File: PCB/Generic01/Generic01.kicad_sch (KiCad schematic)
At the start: 3 parts, among them J1 Header, U1 ESP32-PICO-MINI-02

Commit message: Production files
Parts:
- J1: JLCPCB Position Offset (none) -> 3.81,-1.27; JLCPCB Rotation Offset (none) -> 90; LCSC Part # (none) -> v

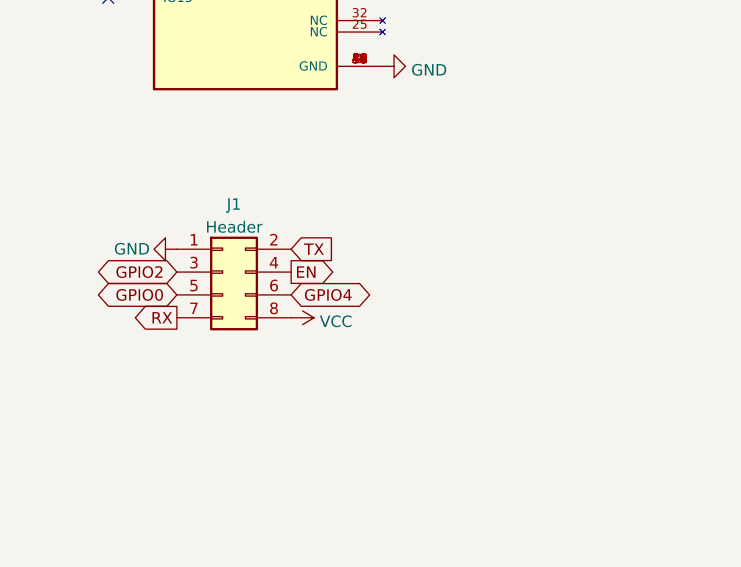
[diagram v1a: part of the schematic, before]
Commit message: Move RST
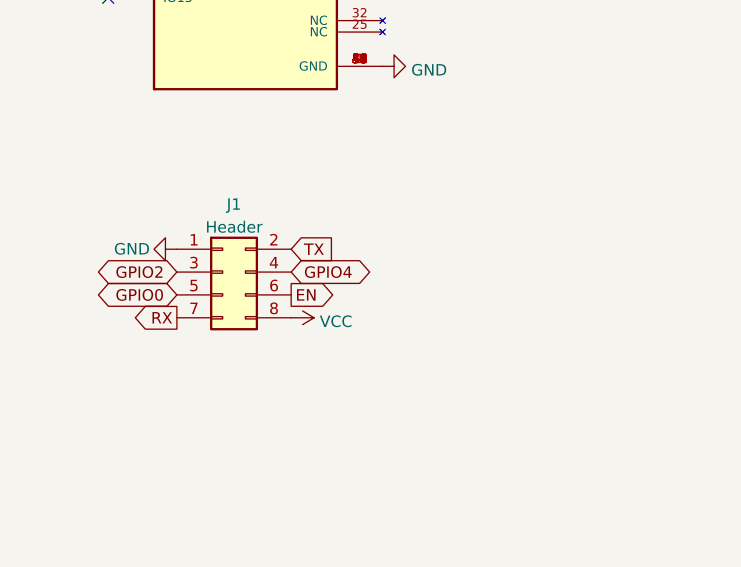
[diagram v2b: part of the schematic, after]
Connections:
- net EN: now also J1.6 (Pin_6); no longer J1.4 (Pin_4)
- net GPIO4: now also J1.4 (Pin_4); no longer J1.6 (Pin_6)
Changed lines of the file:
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@@
     )
   )
-  (global_label "EN" (shape output) (at 129.54 132.08 0) (fields_autoplaced)
+  (global_label "EN" (shape output) (at 129.54 134.62 0) (fields_autoplaced)
     (effects (font (size 1.27 1.27)) (justify left))
-    (property "Intersheetrefs" "${INTERSHEET_REFS}" (at 134.3437 132.0006 0)
+    (property "Intersheetrefs" "${INTERSHEET_REFS}" (at 134.3437 134.5406 0)
       (effects (font (size 1.27 1.27)) (justify left) hide)
     )
@@
     )
   )
-  (global_label "GPIO4" (shape bidirectional) (at 129.54 134.62 0) (fields_autoplaced)
+  (global_label "GPIO4" (shape bidirectional) (at 129.54 132.08 0) (fields_autoplaced)
     (effects (font (size 1.27 1.27)) (justify left))
-    (property "Intersheetrefs" "${INTERSHEET_REFS}" (at 137.549 134.6994 0)
+    (property "Intersheetrefs" "${INTERSHEET_REFS}" (at 137.549 132.1594 0)
       (effects (font (size 1.27 1.27)) (justify left) hide)
     )

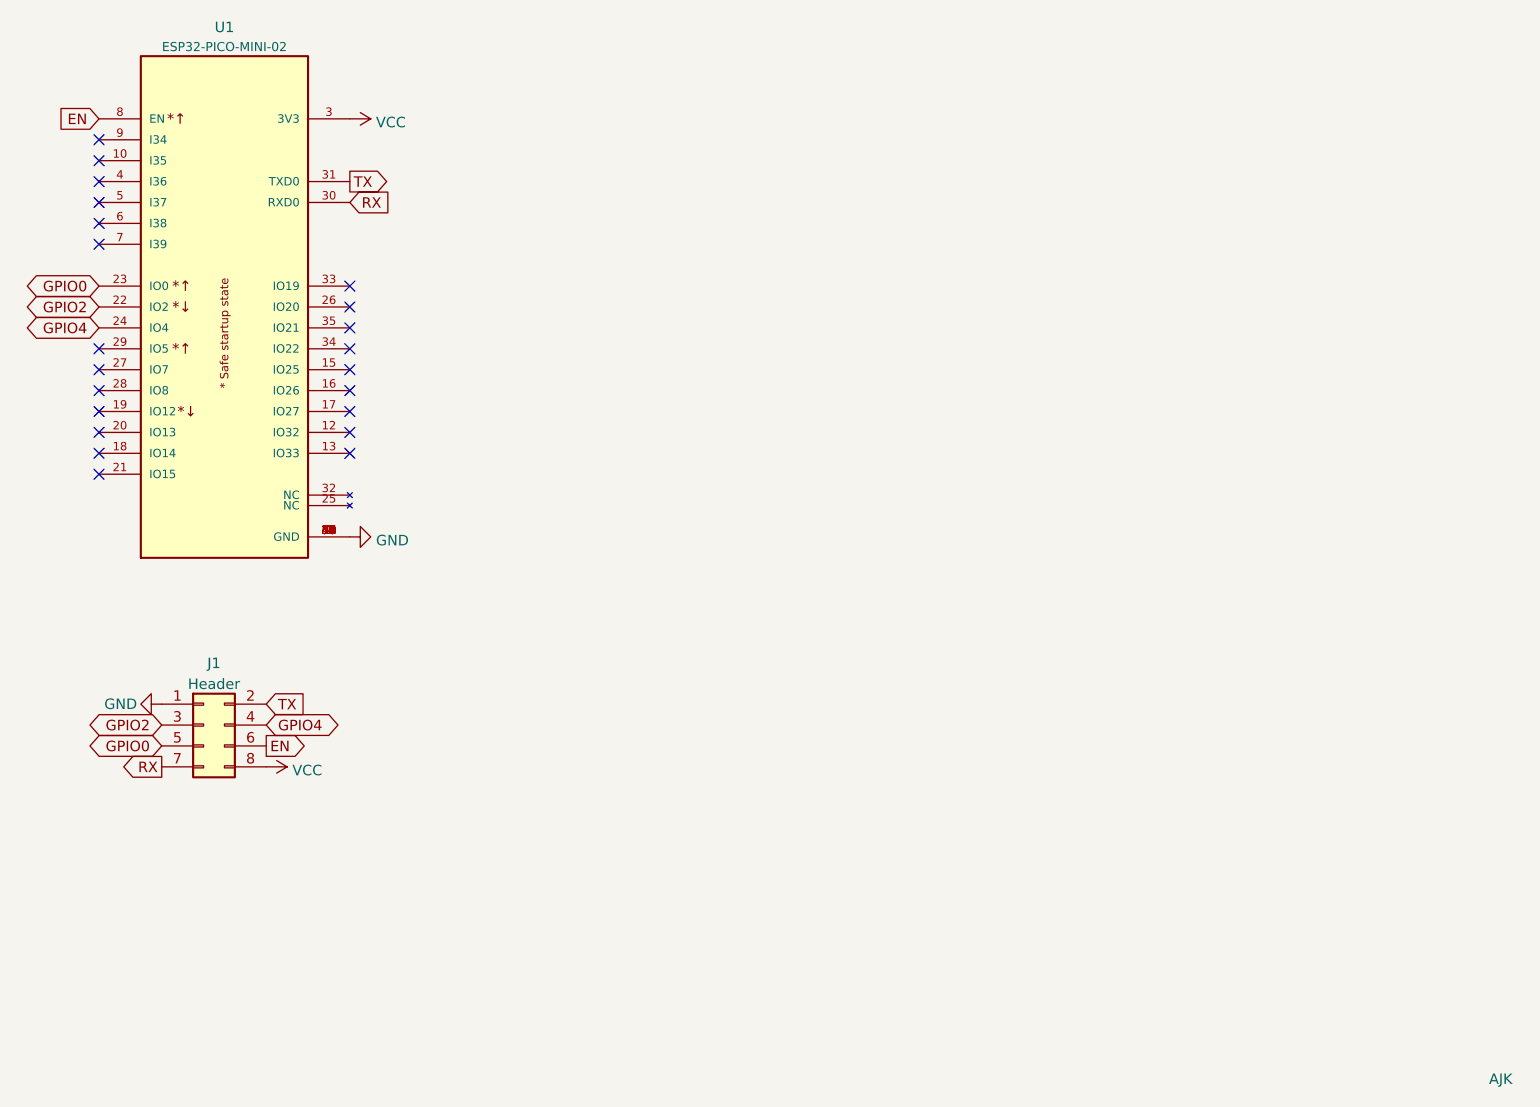
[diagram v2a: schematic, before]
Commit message: Tidy RST as EN
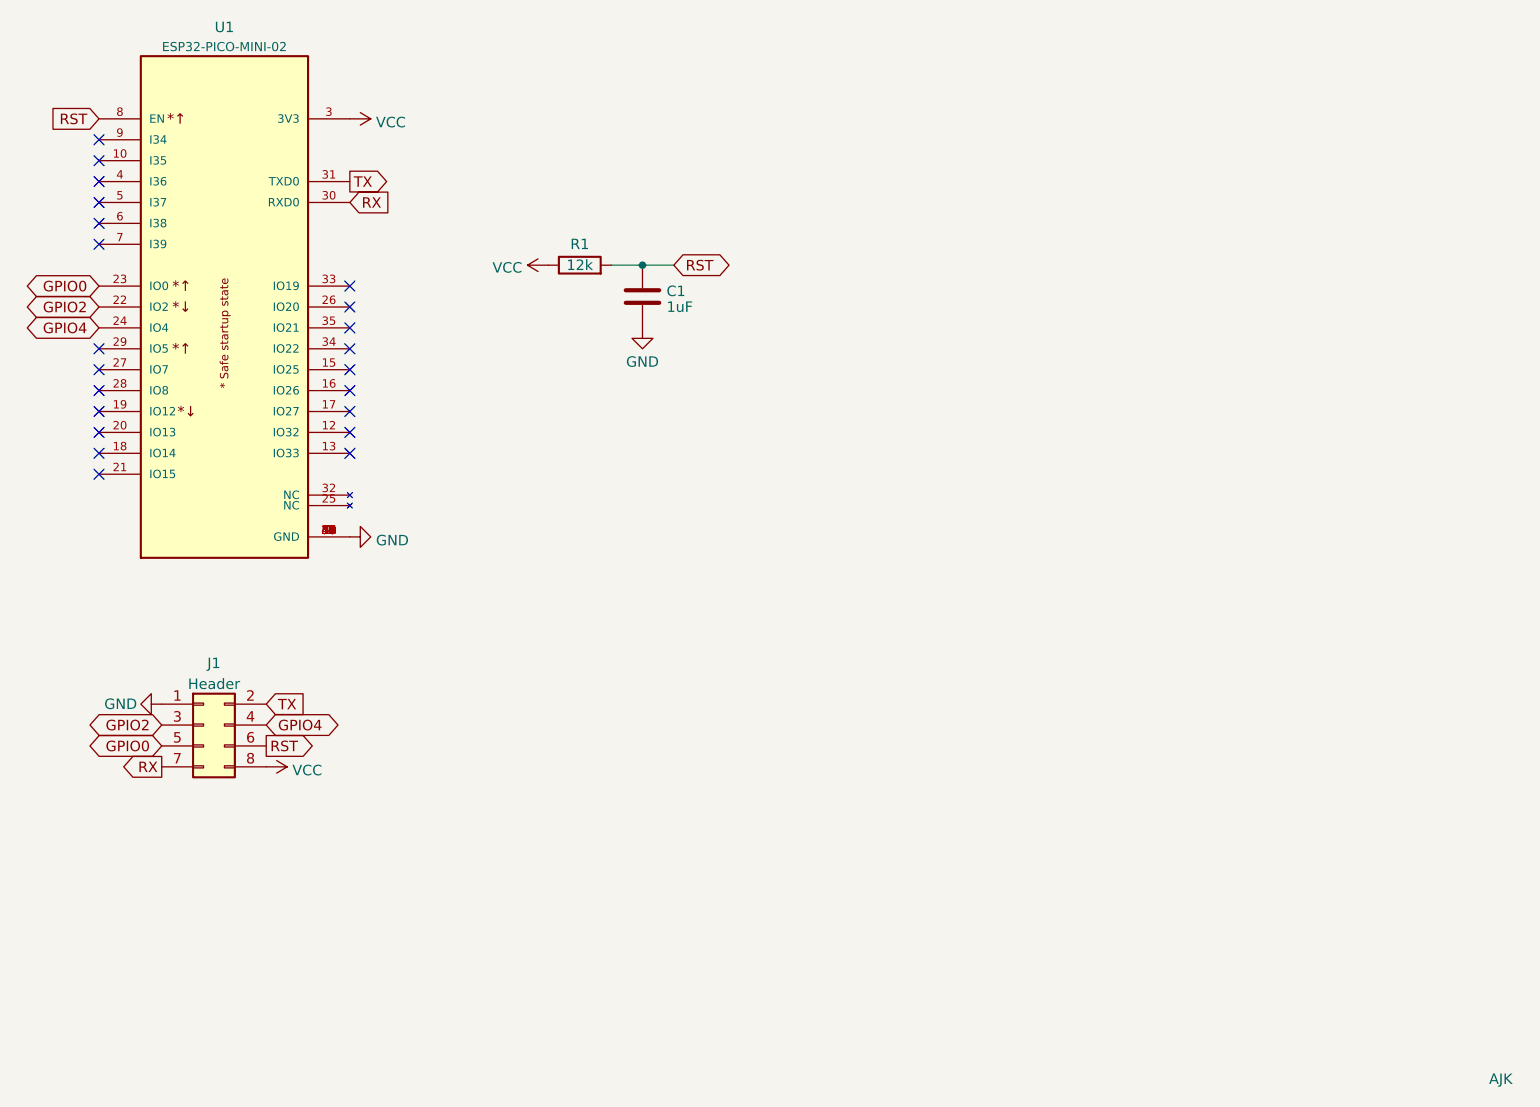
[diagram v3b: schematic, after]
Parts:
- added C1: 1uF, RevK:C_0603, symbol Device:C
- added R1: 12k, RevK:R_0603, symbol Device:R
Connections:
- net GND: now also C1.2
- net VCC: now also R1.1
- net EN renamed RST
- net RST: now also C1.1, R1.2
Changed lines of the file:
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@@
     (comment 2 "www.me.uk")
+  )
+  (junction (at 175.26 76.2) (diameter 0) (color 0 0 0 0)
   )
   (no_connect (at 139.7 99.06))
@@
   (no_connect (at 109.22 63.5))
   (no_connect (at 109.22 60.96))
+  (wire (pts (xy 175.26 76.2) (xy 171.45 76.2))
+    (stroke (width 0) (type default))
+  )
+  (wire (pts (xy 179.07 76.2) (xy 175.26 76.2))
+    (stroke (width 0) (type default))
+  )
   (global_label "TX" (shape input) (at 129.54 129.54 0) (fields_autoplaced)
     (effects (font (size 1.27 1.27)) (justify left))
@@
     )
   )
-  (global_label "EN" (shape output) (at 129.54 134.62 0) (fields_autoplaced)
-    (effects (font (size 1.27 1.27)) (justify left))
-    (property "Intersheetrefs" "${INTERSHEET_REFS}" (at 134.3437 134.5406 0)
+  (global_label "RST" (shape output) (at 129.54 134.62 0) (fields_autoplaced)
+    (effects (font (size 1.27 1.27)) (justify left))
+    (property "Intersheetrefs" "${INTERSHEET_REFS}" (at 135.2387 134.62 0)
       (effects (font (size 1.27 1.27)) (justify left) hide)
     )
@@
     )
   )
-  (global_label "EN" (shape input) (at 109.22 58.42 180) (fields_autoplaced)
-    (effects (font (size 1.27 1.27)) (justify right))
-    (property "Intersheetrefs" "${INTERSHEET_REFS}" (at 104.4163 58.3406 0)
+  (global_label "RST" (shape bidirectional) (at 179.07 76.2 0) (fields_autoplaced)
+    (effects (font (size 1.27 1.27)) (justify left))
+    (property "Intersheetrefs" "${INTERSHEET_REFS}" (at 185.7212 76.2 0)
+      (effects (font (size 1.27 1.27)) (justify left) hide)
+    )
+  )
+  (global_label "RST" (shape input) (at 109.22 58.42 180) (fields_autoplaced)
+    (effects (font (size 1.27 1.27)) (justify right))
+    (property "Intersheetrefs" "${INTERSHEET_REFS}" (at 103.5213 58.42 0)
       (effects (font (size 1.27 1.27)) (justify right) hide)
     )
@@
     (property "Intersheetrefs" "${INTERSHEET_REFS}" (at 144.2013 65.9606 0)
       (effects (font (size 1.27 1.27)) (justify left) hide)
+    )
+  )
+  (symbol (lib_id "Device:R") (at 167.64 76.2 90) (unit 1)
+    (in_bom yes) (on_board yes) (dnp no)
+    (property "Reference" "R1" (at 167.64 73.66 90)
+      (effects (font (size 1.27 1.27)))
+    )
+    (property "Value" "12k" (at 167.64 76.2 90)
+      (effects (font (size 1.27 1.27)))
+    )
+    (property "Footprint" "RevK:R_0603" (at 167.64 77.978 90)
+      (effects (font (size 1.27 1.27)) hide)
+    )
+    (property "Datasheet" "~" (at 167.64 76.2 0)
+      (effects (font (size 1.27 1.27)) hide)
+    )
+    (pin "1")
+    (pin "2")
+    (instances
+      (project "Generic01"
+        (path "/46c350bb-7de4-4e81-aafd-4af55e37aab0"
+          (reference "R1") (unit 1)
+        )
+      )
     )
   )
@@
         (path "/46c350bb-7de4-4e81-aafd-4af55e37aab0"
           (reference "#PWR01") (unit 1)
+        )
+      )
+    )
+  )
+  (symbol (lib_id "power:VCC") (at 163.83 76.2 90) (unit 1)
+    (in_bom yes) (on_board yes) (dnp no) (fields_autoplaced)
+    (property "Reference" "#PWR05" (at 167.64 76.2 0)
+      (effects (font (size 1.27 1.27)) hide)
+    )
+    (property "Value" "VCC" (at 160.655 76.5168 90)
+      (effects (font (size 1.27 1.27)) (justify left))
+    )
+    (property "Footprint" "" (at 163.83 76.2 0)
+      (effects (font (size 1.27 1.27)) hide)
+    )
+    (property "Datasheet" "" (at 163.83 76.2 0)
+      (effects (font (size 1.27 1.27)) hide)
+    )
+    (pin "1")
+    (instances
+      (project "Generic01"
+        (path "/46c350bb-7de4-4e81-aafd-4af55e37aab0"
+          (reference "#PWR05") (unit 1)
         )
       )
@@
     )
   )
+  (symbol (lib_id "power:GND") (at 175.26 83.82 0) (unit 1)
+    (in_bom yes) (on_board yes) (dnp no) (fields_autoplaced)
+    (property "Reference" "#PWR06" (at 175.26 90.17 0)
+      (effects (font (size 1.27 1.27)) hide)
+    )
+    (property "Value" "GND" (at 175.26 87.9555 0)
+      (effects (font (size 1.27 1.27)))
+    )
+    (property "Footprint" "" (at 175.26 83.82 0)
+      (effects (font (size 1.27 1.27)) hide)
+    )
+    (property "Datasheet" "" (at 175.26 83.82 0)
+      (effects (font (size 1.27 1.27)) hide)
+    )
+    (pin "1")
+    (instances
+      (project "Generic01"
+        (path "/46c350bb-7de4-4e81-aafd-4af55e37aab0"
+          (reference "#PWR06") (unit 1)
+        )
+      )
+    )
+  )
   (symbol (lib_id "power:VCC") (at 129.54 137.16 270) (unit 1)
     (in_bom yes) (on_board yes) (dnp no) (fields_autoplaced)
@@
         )
       )
+    )
+  )
+  (symbol (lib_id "Device:C") (at 175.26 80.01 0) (unit 1)
+    (in_bom yes) (on_board yes) (dnp no) (fields_autoplaced)
+    (property "Reference" "C1" (at 178.181 79.3663 0)
+      (effects (font (size 1.27 1.27)) (justify left))
+    )
+    (property "Value" "1uF" (at 178.181 81.2873 0)
+      (effects (font (size 1.27 1.27)) (justify left))
+    )
+    (property "Footprint" "RevK:C_0603" (at 176.2252 83.82 0)
+      (effects (font (size 1.27 1.27)) hide)
+    )
+    (property "Datasheet" "~" (at 175.26 80.01 0)
+      (effects (font (size 1.27 1.27)) hide)
+    )
+    (pin "1")
+    (pin "2")
+    (instances
+      (project "Generic01"
+        (path "/46c350bb-7de4-4e81-aafd-4af55e37aab0"
+          (reference "C1") (unit 1)
+        )
+      )

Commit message: PCB Update
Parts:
- J1: JLCPCB Position Offset 3.81,-1.27 -> (none); JLCPCB Rotation Offset 90 -> (none); LCSC Part # v -> (none)
